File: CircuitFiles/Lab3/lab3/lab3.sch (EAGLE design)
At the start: 18 parts, among them SW1 CT10-XXXX-A2, SW2 CT10-XXXX-A2, SW3 CT10-XXXX-A2, SW4 CT10-XXXX-A2, SW5 CT10-XXXX-A2

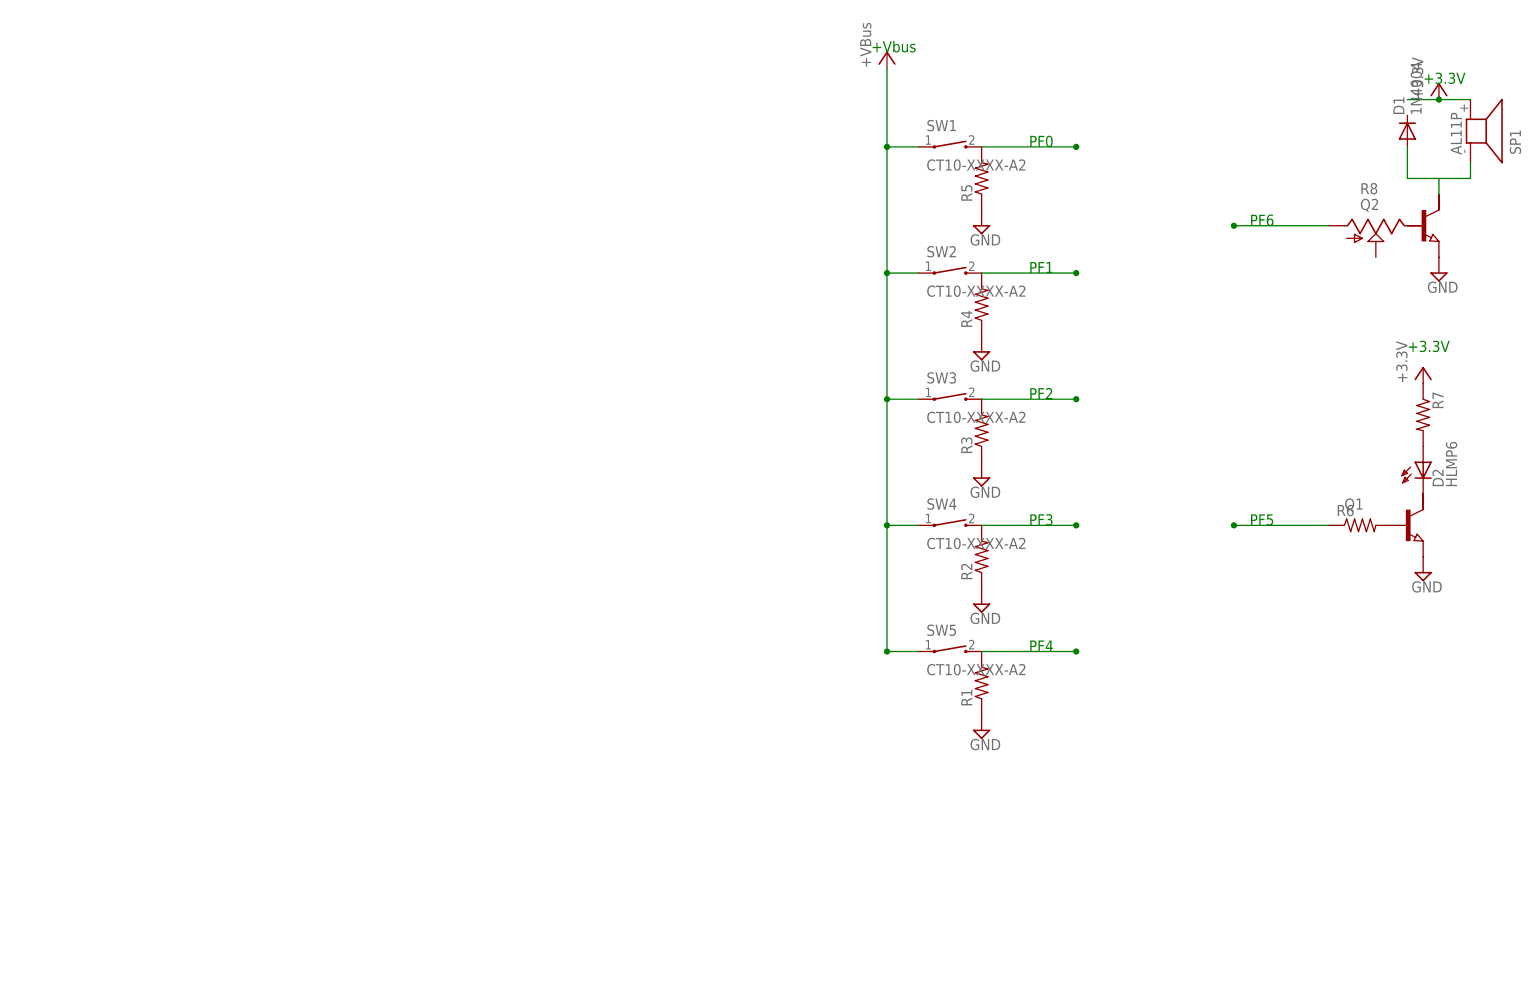
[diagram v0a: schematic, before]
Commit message: Adding final submitted circuit for Lab 3
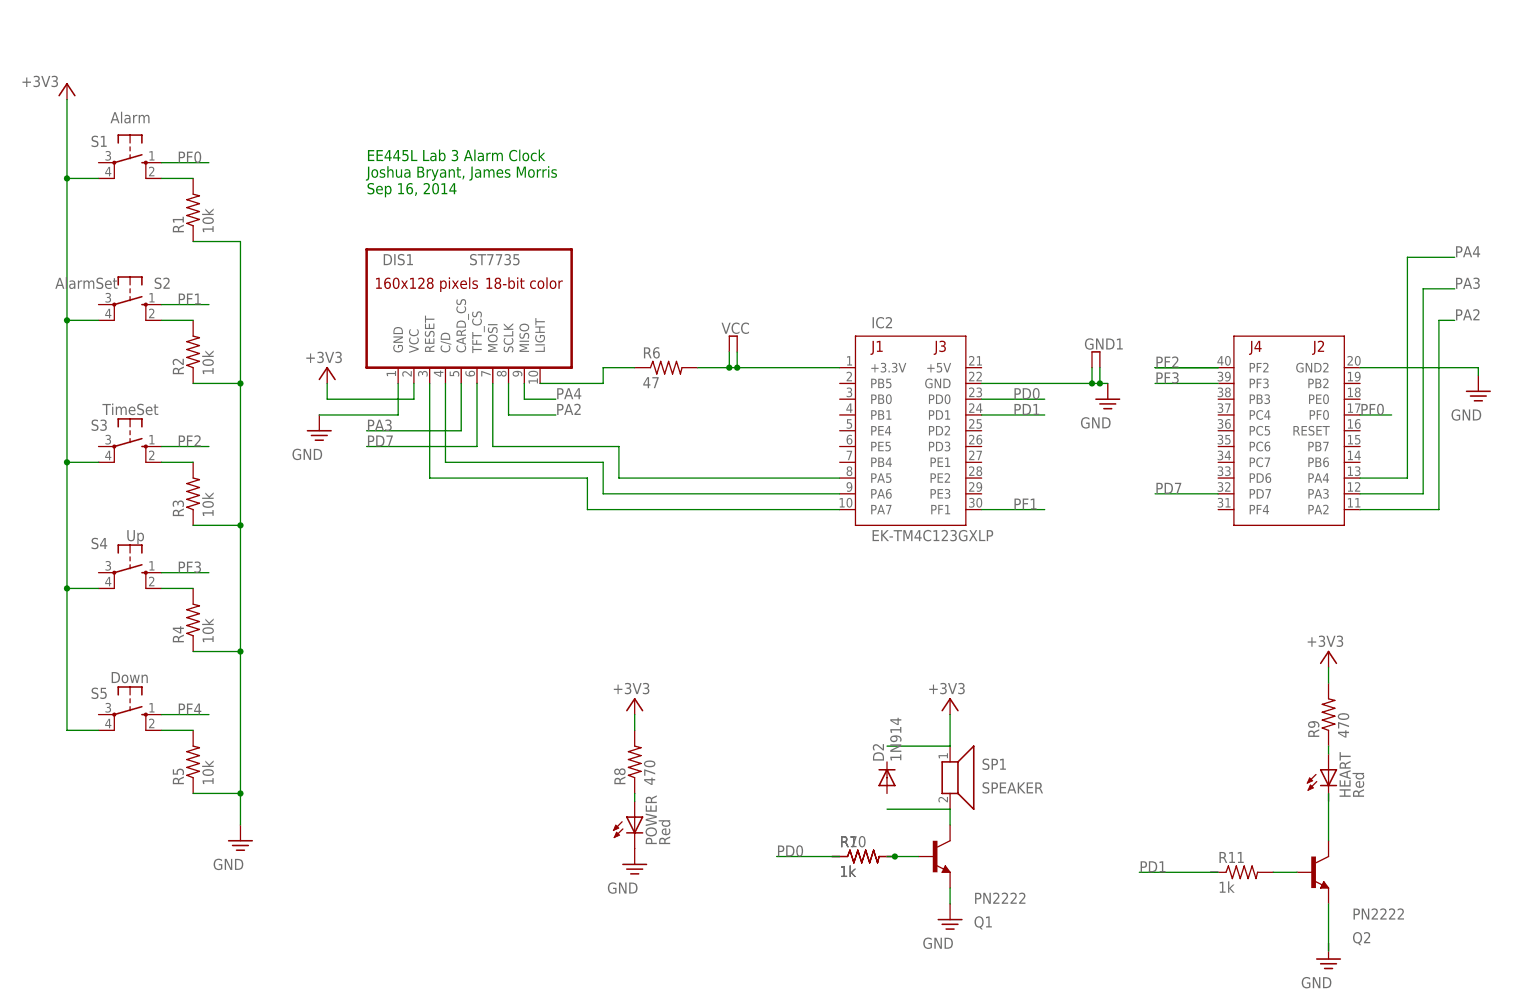
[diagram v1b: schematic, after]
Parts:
- removed D1: 1N4004, diode:1N4004
- removed SW1, SW2, SW3, SW4, SW5: CT10-XXXX-A2, switch-coto:CT10-XXXX-A2
- added DIS1: ST7735, EE445L:ST7735
- added GND1, VCC: TP2, EE445L:TP2
- added HEART, POWER: Red, EE445L:LED5MM
- added IC2: EK-TM4C123GXLP, EE445L:EK-TM4C123GXLP
- added R10, R11: 1k, EE445L:RESISTOR0204/5
- added R9: 470, EE445L:RESISTOR0204/5
- added S1: Alarm, EE445L:B3F-1052
- added S2: AlarmSet, EE445L:B3F-1052
- added S3: TimeSet, EE445L:B3F-1052
- added S4: Up, EE445L:B3F-1052
- added S5: Down, EE445L:B3F-1052
- D2: value HLMP6 -> 1N914; device display-hp:HLMP6 -> diode:1N5060GP
- Q1, Q2: value (none) -> PN2222; device semicon-smd-ipc:NPN-TRANSISTIOR-2COLSOT89 -> EE445L:PN2222
- R1, R2, R3, R4, R5: value (none) -> 10k; device rcl:R-US_0204/7 -> EE445L:RESISTOR0204/5
- R6: value (none) -> 47; device rcl:R-US_0204/5 -> EE445L:RESISTORV526-0
- R7: value (none) -> 1k; device rcl:R-US_0204/5 -> EE445L:RESISTOR0204/5
- R8: value (none) -> 470; device pot:TRIM_US-B25U -> EE445L:RESISTOR0204/5
- SP1: value AL11P -> SPEAKER; device buzzer:AL11P -> EE445L:SPEAKER
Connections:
- removed net VCC: R7.1, SP1.2, SW1.1, SW2.1, SW3.1, SW4.1, SW5.1
- new net +3V3: DIS1.VCC, R8.2, R9.2, S1.P1, S2.P1, S3.P1, S4.P1, S5.P1, SP1.1
- new net LIGHT: DIS1.LIGHT, R6.1
- new net N$10: Q2.C
- new net N$11: R10.1, R7.1
- new net N$12: Q2.B, R11.2
- new net PA2: DIS1.SCLK, IC2.PA2
- new net PA3: DIS1.CARD_CS, IC2.PA3
- new net PA4: DIS1.MISO, IC2.PA4
- new net PA5: DIS1.MOSI, IC2.PA5
- new net PA6: DIS1.C/D, IC2.PA6
- new net PA7: DIS1.RESET, IC2.PA7
- new net PD0: IC2.PD0
- new net PD1: IC2.PD1
- new net PD7: DIS1.TFT_CS, IC2.PD7
- new net PF0: IC2.PF0, S1.S
- new net PF1: S2.S
- new net PF2: IC2.PF2, S3.S
- new net PF3: S4.S
- new net PF4: S5.S
- new net VLED: POWER.A, R8.1
- new net VLED1: HEART.A, R9.1
- net GND: now also DIS1.GND, GND1.TPA, GND1.TPB, IC2.GND, IC2.GND2, POWER.C; no longer Q2.E
- net N$1: now also IC2.+3.3V, R6.2, VCC.TPA, VCC.TPB; no longer R2.2, SW4.2
- net N$2: now also S1.S1; no longer SW5.2
- net N$3: now also R2.2, S2.S1; no longer R3.2, SW3.2
- net N$4: now also R3.2, S3.S1; no longer R4.2, SW2.2
- net N$5: now also R4.2, S4.S1; no longer R5.2, R8.A, SW1.2
- net N$6: now also R5.2, S5.S1; no longer Q1.B, R6.2
- net N$7: now also Q1.B, R10.2, R7.2; no longer D2.K, Q1.C
- net N$8: now also Q1.C, SP1.2; no longer D2.A, R7.2
- net N$9: now also Q2.E; no longer D1.A, Q2.C, SP1.1
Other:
- note added: "EE445L Lab 3 Alarm Clock Joshua Bryant, James Morris Sep 16, 2014"
- note removed: "+3.3V"
- note removed: "+Vbus"
- note removed: "PF0"
- note removed: "PF1"
- note removed: "PF2"
- note removed: "PF3"
- note removed: "PF4"
- note removed: "PF5"
- note removed: "PF6"
- moved on the sheet: R1, R2, R3, R4, R5, R6, R7
